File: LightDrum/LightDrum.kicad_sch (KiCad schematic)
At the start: 31 parts, among them J102 JTAG, Q101 RQ5A030AP, SW101 SW_SPDT, U101 STM32F103VEH6, U102 24LC04, Y101 8MHz, Y102 32.768KHz

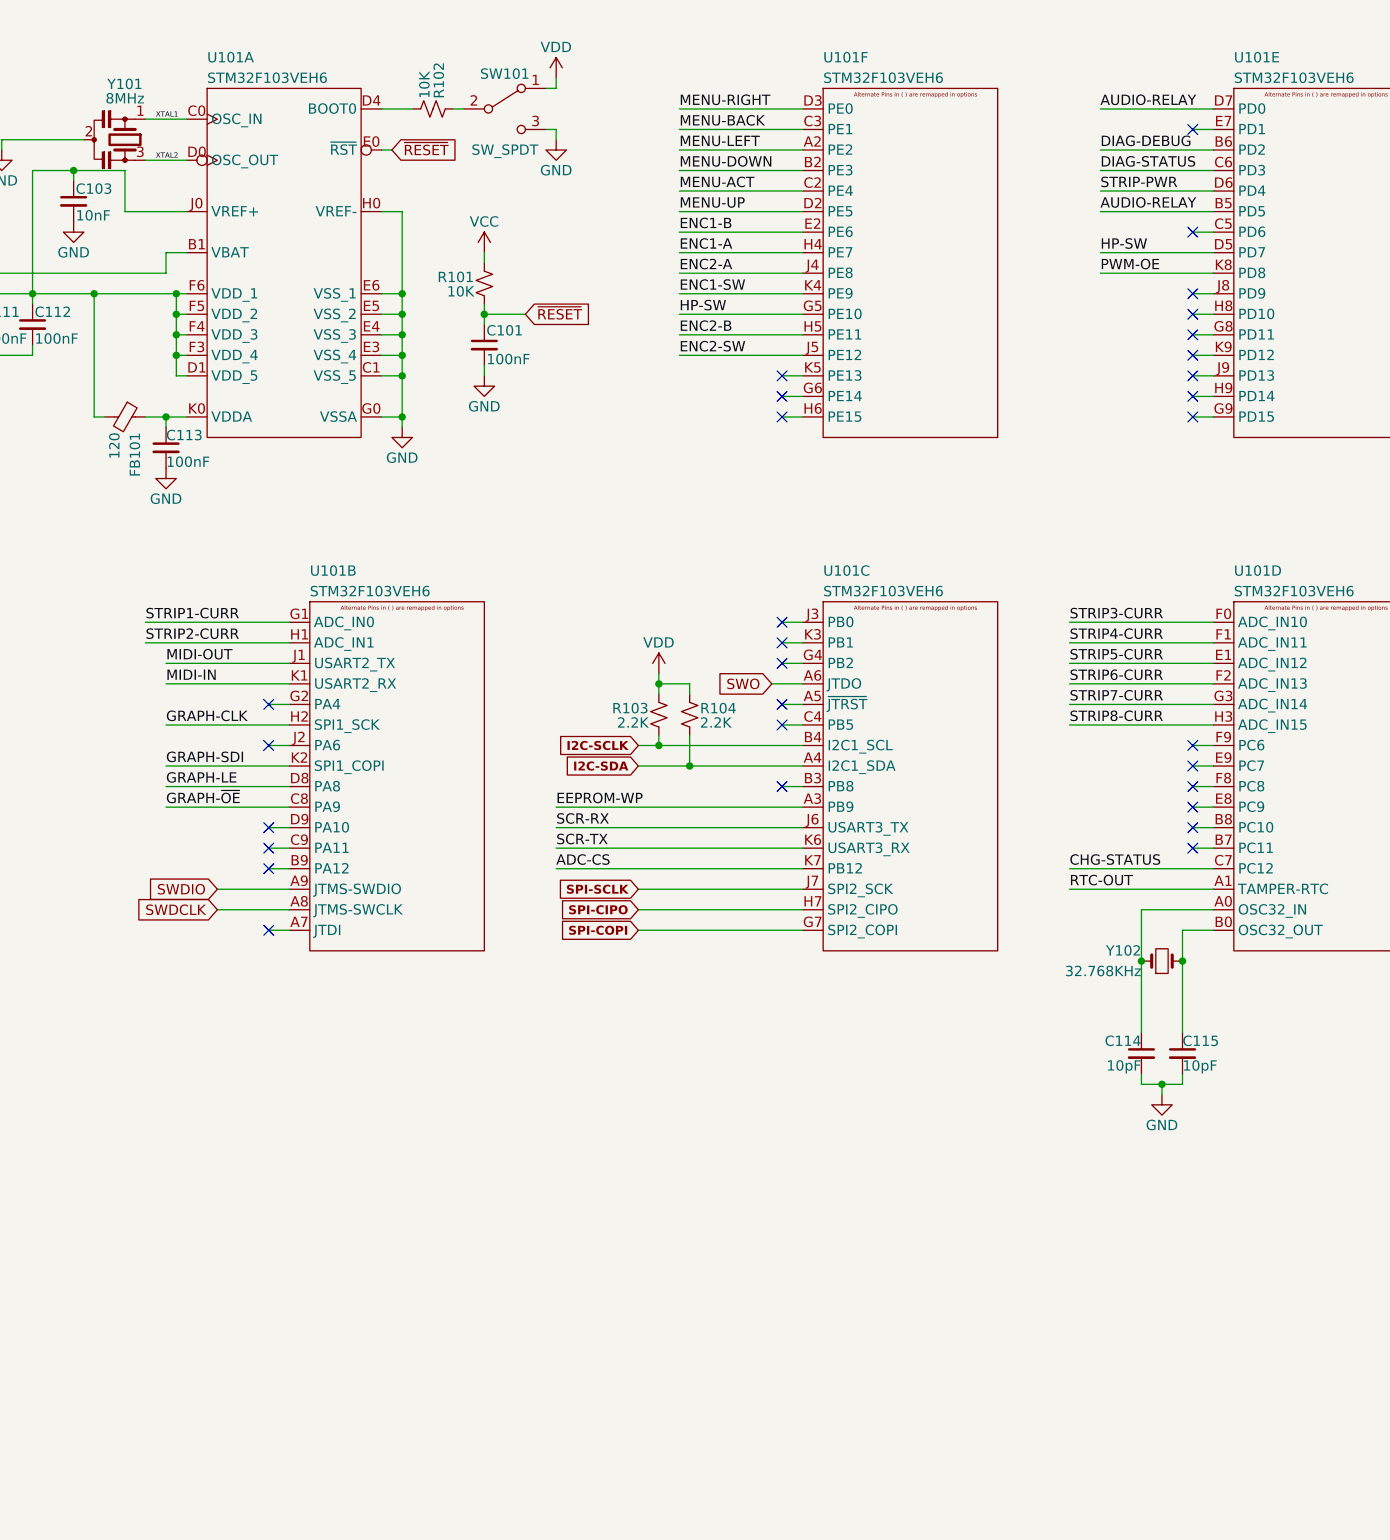
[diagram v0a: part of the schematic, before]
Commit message: Replace with smaller case (WIP)
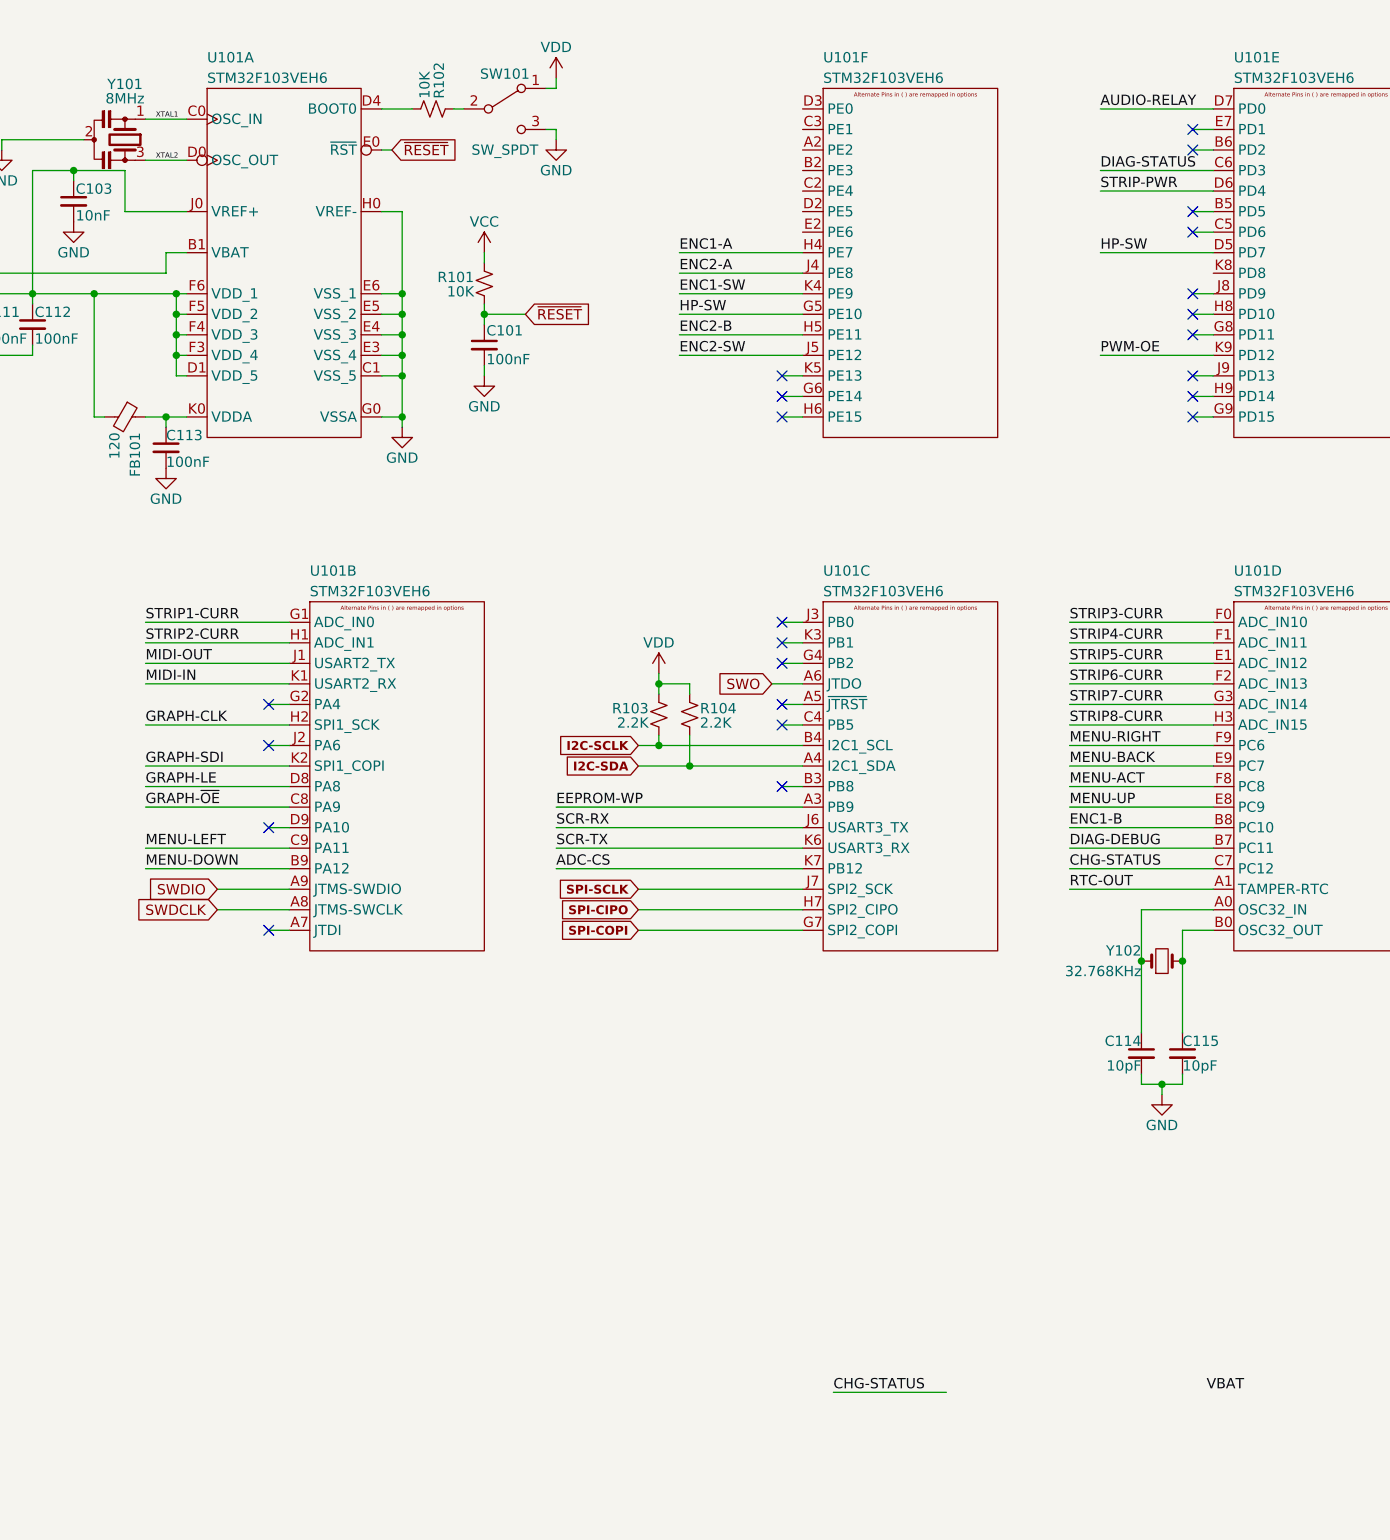
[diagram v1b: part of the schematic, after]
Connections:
- net AUDIO-RELAY: no longer U101.B5 (PD5)
- net DIAG-DEBUG: now also U101.B7 (PC11); no longer U101.B6 (PD2)
- net ENC1-B: now also U101.B8 (PC10); no longer U101.E2 (PE6)
- net MENU-ACT: now also U101.F8 (PC8); no longer U101.C2 (PE4)
- net MENU-BACK: now also U101.E9 (PC7); no longer U101.C3 (PE1)
- net MENU-DOWN: now also U101.B9 (PA12); no longer U101.B2 (PE3)
- net MENU-LEFT: now also U101.C9 (PA11); no longer U101.A2 (PE2)
- net MENU-RIGHT: now also U101.F9 (PC6); no longer U101.D3 (PE0)
- net MENU-UP: now also U101.E8 (PC9); no longer U101.D2 (PE5)
- net PWM-OE: now also U101.K9 (PD12); no longer U101.K8 (PD8)
- no-connect marks 31 -> 24

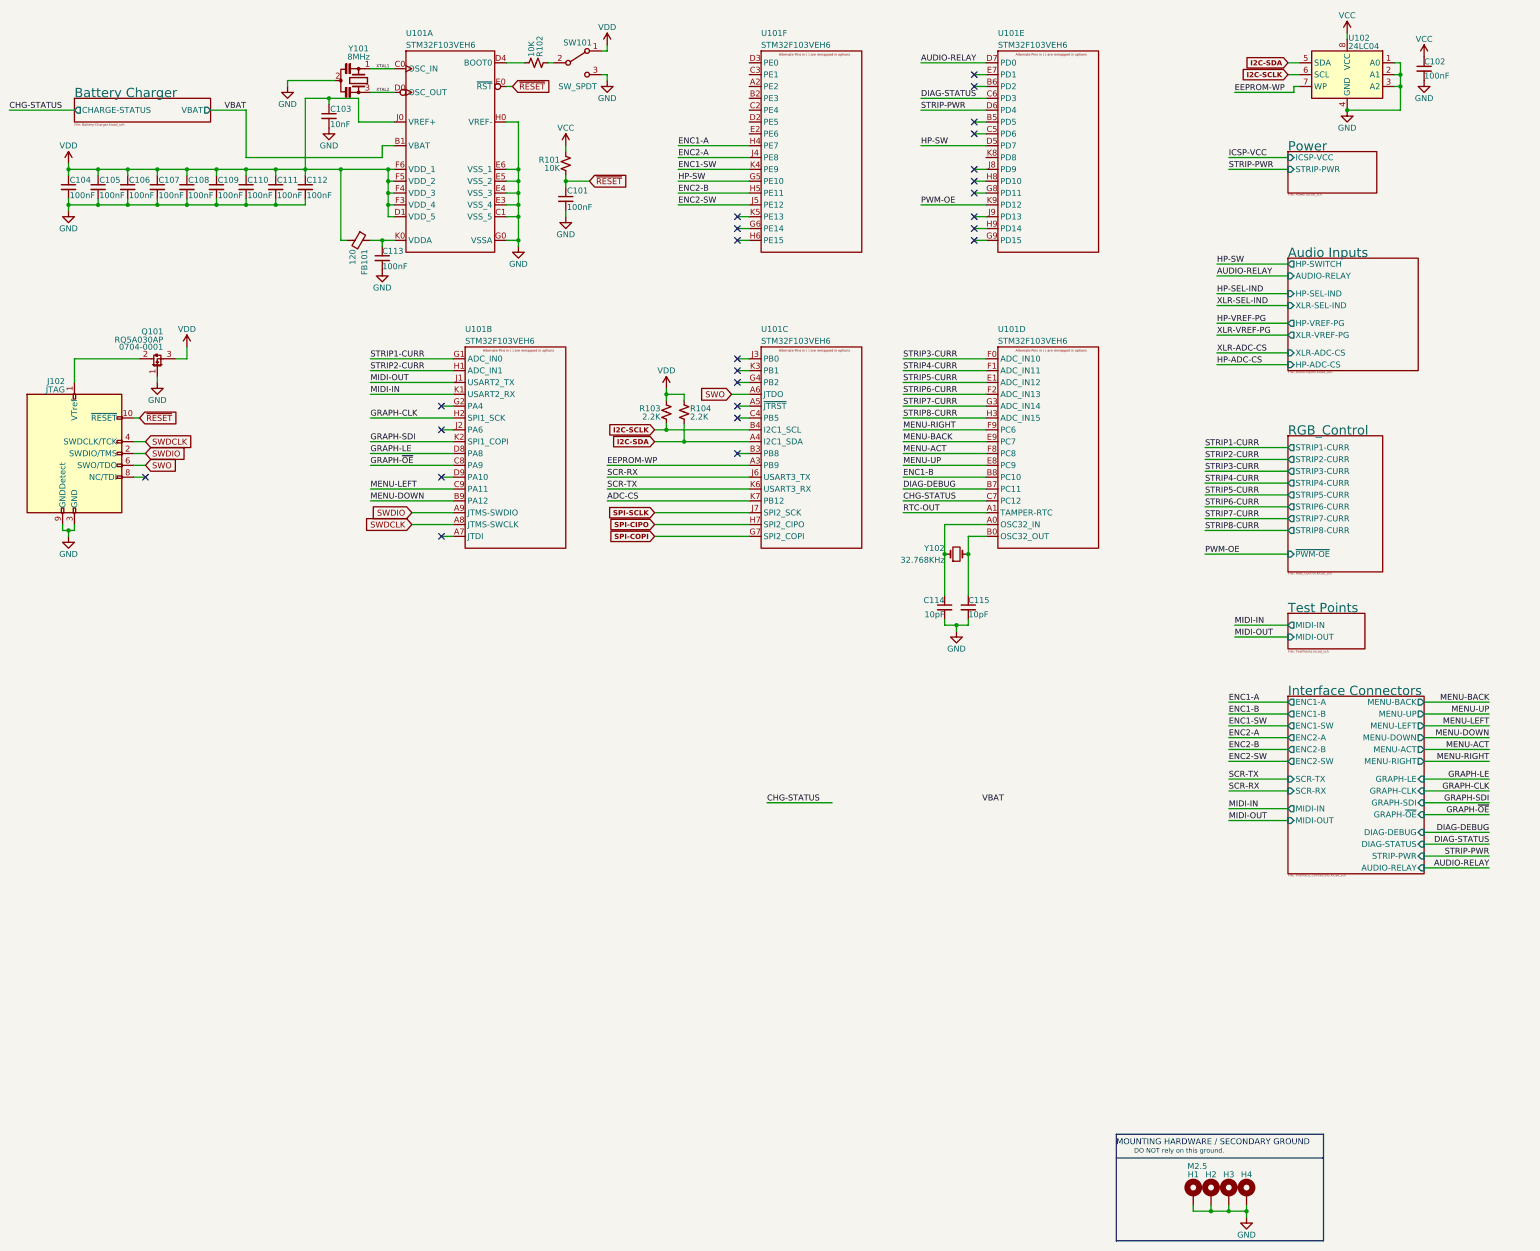
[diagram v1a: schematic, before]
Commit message: Simplify analog power supply and add some routing
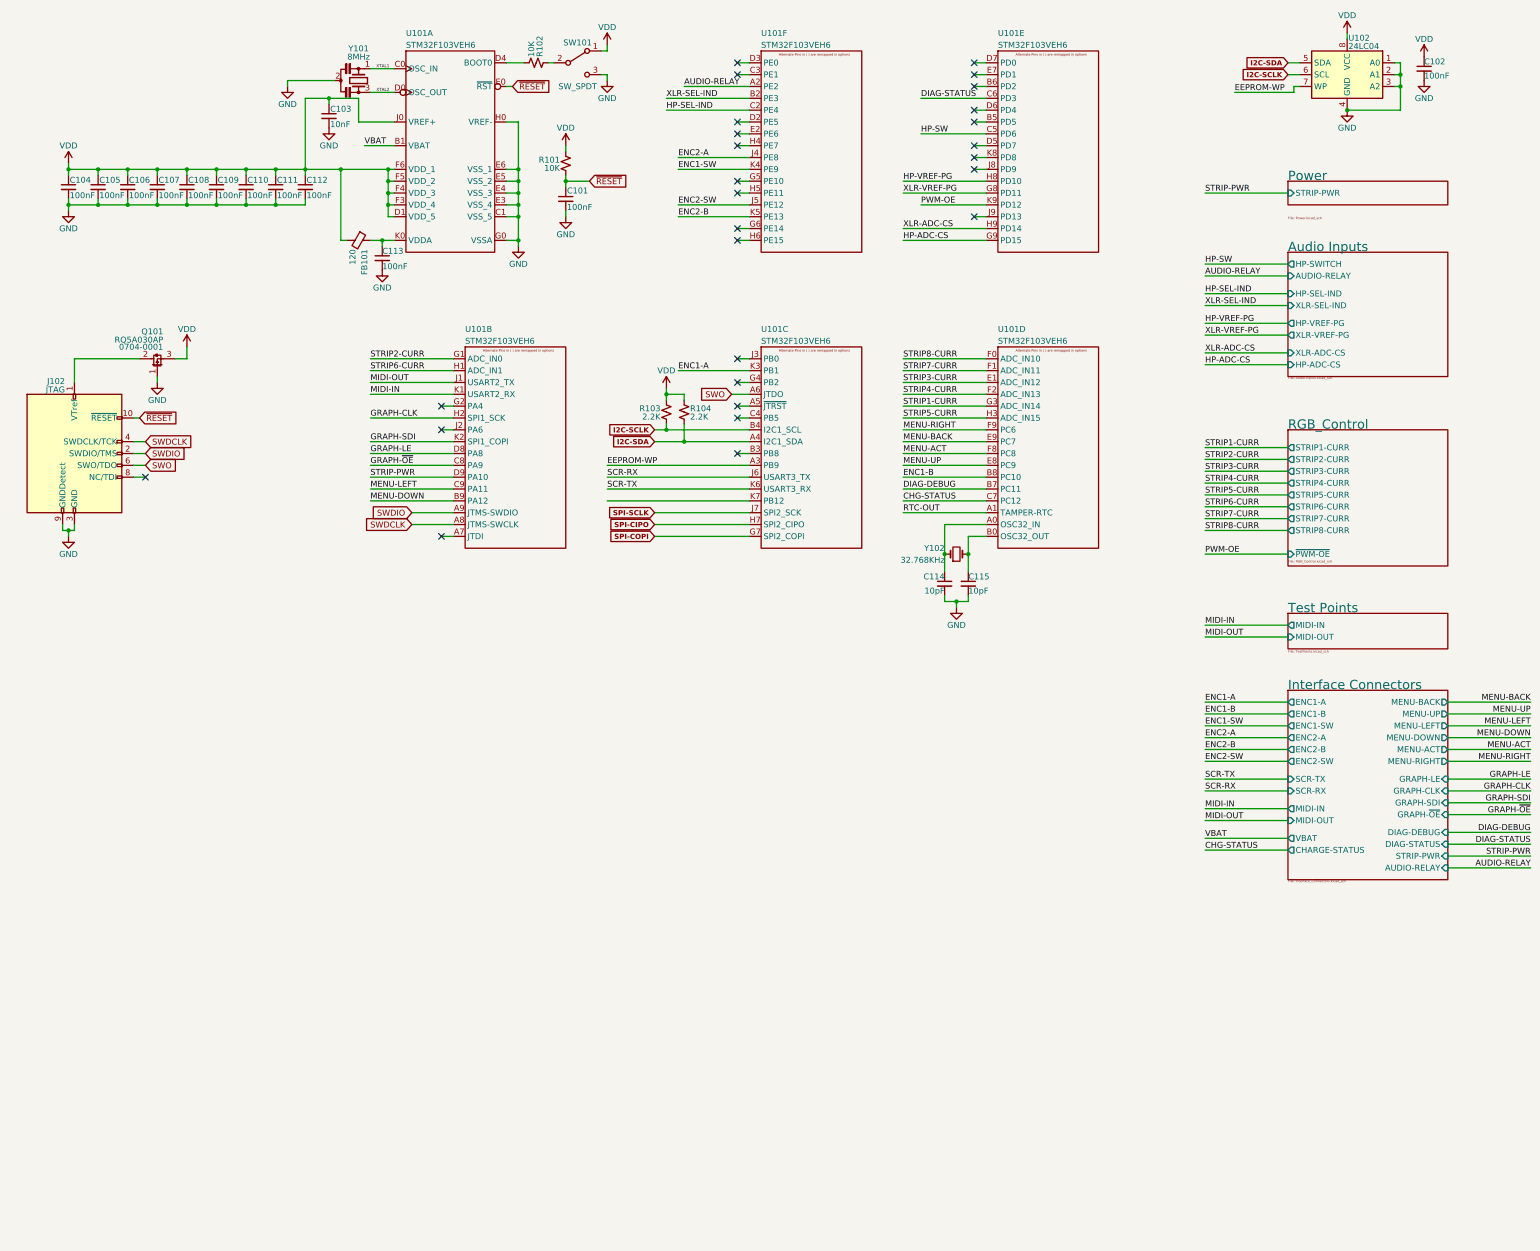
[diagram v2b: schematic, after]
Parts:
- removed H1, H2, H3, H4: M2.5, MountingHole:MountingHole_2.5mm_Pad, symbol Mechanical:MountingHole_Pad
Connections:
- net VCC is gone; now on net VDD: C102.1, R101.1, U102.8 (VCC)
- net AUDIO-RELAY: now also U101.A2 (PE2); no longer U101.D7 (PD0)
- net ENC1-A: now also U101.K3 (PB1); no longer U101.H4 (PE7)
- net ENC2-B: now also U101.K5 (PE13); no longer U101.H5 (PE11)
- net HP-ADC-CS: now also U101.G9 (PD15)
- net HP-SEL-IND: now also U101.C2 (PE4)
- net HP-SW: now also U101.C5 (PD6); no longer U101.D5 (PD7), U101.G5 (PE10)
- net HP-VREF-PG: now also U101.H8 (PD10)
- net STRIP-PWR: now also U101.D9 (PA10); no longer U101.D6 (PD4)
- net STRIP1-CURR: now also U101.G3 (PC4); no longer U101.G1 (PA0)
- net STRIP2-CURR: now also U101.G1 (PA0); no longer U101.H1 (PA1)
- net STRIP3-CURR: now also U101.E1 (PC2); no longer U101.F0 (PC0)
- net STRIP4-CURR: now also U101.F2 (PC3); no longer U101.F1 (PC1)
- net STRIP5-CURR: now also U101.H3 (PC5); no longer U101.E1 (PC2)
- net STRIP6-CURR: now also U101.H1 (PA1); no longer U101.F2 (PC3)
- net STRIP7-CURR: now also U101.F1 (PC1); no longer U101.G3 (PC4)
- net STRIP8-CURR: now also U101.F0 (PC0); no longer U101.H3 (PC5)
- net XLR-ADC-CS: now also U101.H9 (PD14)
- net XLR-SEL-IND: now also U101.B2 (PE3)
- net XLR-VREF-PG: now also U101.G8 (PD11)
- net ADC-CS: no longer names the net of U101.K7 (PB12)
- no-connect marks 24 -> 27
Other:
- removed sheet Battery Charger
- sheet Interface Connectors ports: added CHARGE-STATUS, VBAT; removed none
- sheet Power ports: added none; removed ICSP-VCC
- note removed: "DO NOT rely on this ground."
- note removed: "MOUNTING HARDWARE / SECONDARY GROUND"
- moved on the sheet: C114, C115
